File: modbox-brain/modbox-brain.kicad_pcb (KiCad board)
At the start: 2 copper layers, 100 x 40 mm, 30 parts, among them P1 MICRO-USB-B, P2 CONN_01X04, Q1 Q_PMOS_GDS, Q2 BC237, Q3 BC237, U1 MCP73831T, U2 CP2102

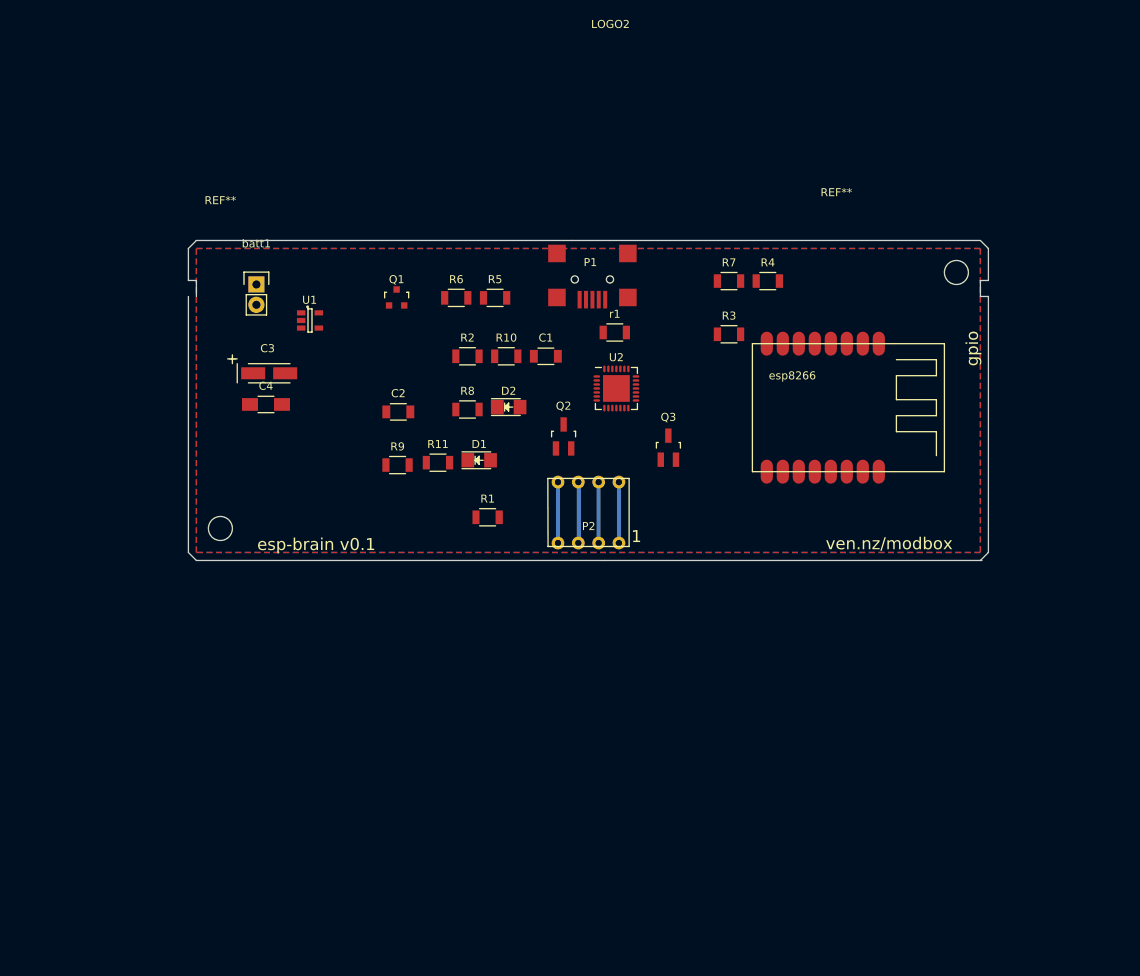
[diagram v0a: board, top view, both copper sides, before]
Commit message: buck converter instead of ldo
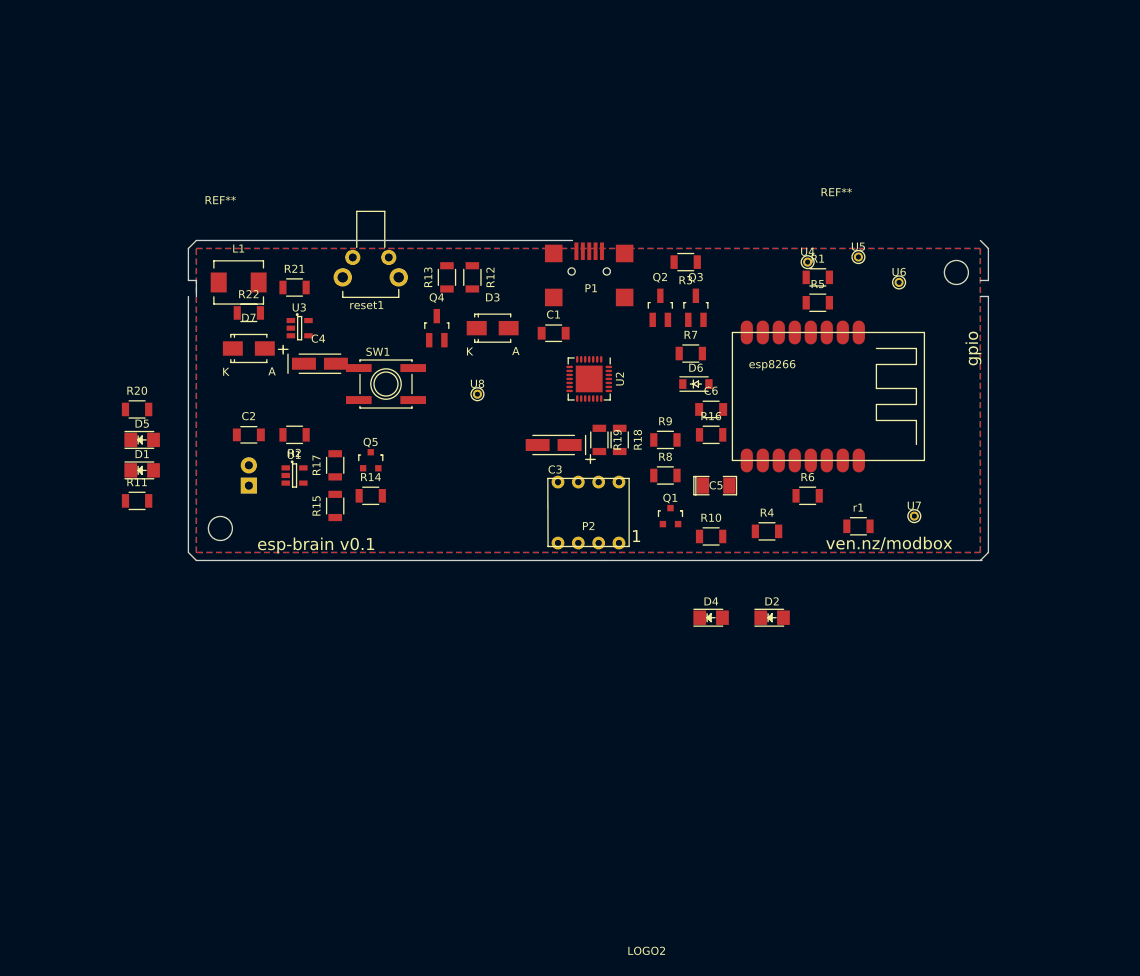
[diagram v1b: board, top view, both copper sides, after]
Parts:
- added C5: 0.1uf, SMD_Packages:SMD-1206_Pol, F.Cu at (181.0, 80.6)
- added C6: 1u, Capacitors_SMD:C_1206, F.Cu at (180.3, 71.1)
- added D3: D_Schottky, Diodes_SMD:SMA_Standard, F.Cu at (153.0, 61.0)
- added D4: low batt, LEDs:LED-1206, F.Cu at (180.3, 97.2)
- added D5: charge complete led, LEDs:LED-1206, F.Cu at (109.2, 74.9)
- added D6: D, Diodes_SMD:SOD-123, F.Cu at (178.4, 67.9)
- added D7: 1.5a, Diodes_SMD:SMA_Standard, F.Cu at (122.6, 63.5)
- added L1: 2.2u 1.8A, Inductors_NEOSID:Neosid_Inductor_SM-PIC0512H, F.Cu at (121.3, 55.2)
- added Q4: Q_PMOS_GSD, Housings_SOT-23_SOT-143_TSOT-6:SOT-23_Handsoldering, F.Cu at (146.1, 61.0)
- added Q5: Q_NMOS_GSD, TO_SOT_Packages_SMD:SOT-23, F.Cu at (137.8, 77.5)
- added R12: 30k, Resistors_SMD:R_1206, F.Cu at (150.5, 54.6)
- added R13: 60k, Resistors_SMD:R_1206, F.Cu at (147.3, 54.6)
- added R14: 10k, Resistors_SMD:R_1206, F.Cu at (137.8, 81.9)
- added R15: 4.7k, Resistors_SMD:R_1206, F.Cu at (133.3, 83.2)
- added R16: 100k, Resistors_SMD:R_1206, F.Cu at (180.3, 74.3)
- added R17: 10k, Resistors_SMD:R_1206, F.Cu at (133.3, 78.1)
- added R18: 4.7k, Resistors_SMD:R_1206, F.Cu at (168.9, 74.9)
- added R19: 4.7k, Resistors_SMD:R_1206, F.Cu at (166.4, 74.9)
- added R20: 500r, Resistors_SMD:R_1206, F.Cu at (108.6, 71.1)
- added R21: 45.3k, Resistors_SMD:R_1206, F.Cu at (128.3, 55.9)
- added R22: 100k, Resistors_SMD:R_1206, F.Cu at (122.6, 59.1)
- added SW1: SW_PUSH, Buttons_Switches_SMD:SW_SPST_EVQQ2, F.Cu at (139.7, 67.9)
- added U3: lmr1501, TO_SOT_Packages_SMD:SOT-23-5, F.Cu at (128.9, 61.0)
- added U4: testpoint, Connect:PINTST, F.Cu at (192.4, 52.7)
- added U5: testpoint, Connect:PINTST, F.Cu at (198.8, 52.1)
- added U6: testpoint, Connect:PINTST, F.Cu at (203.8, 55.2)
- added U7: testpoint, Connect:PINTST, F.Cu at (205.7, 84.5)
- added U8: testpoint, Connect:PINTST, F.Cu at (151.1, 69.2)
- added reset1: SW_PUSH, fp:ra tactile, F.Cu at (137.8, 54.6)
- C3: value 10uf -> 22uf 5v
- C4: value 0.1uf -> 22uf 10v; footprint Capacitors_SMD:C_1206_HandSoldering -> Capacitors_Tantalum_SMD:TantalC_SizeA_EIA-3216_HandSoldering
- D1: value LED -> charging led
- D2: value LED -> wifi status
- R10: value 2k -> 100k
- R9: value 2k -> 68r
- U1: value MCP73831T -> MCP73831
- batt1: moved to B.Cu
- moved LOGO2 115.9 mm to (172.2, 141.3)
- moved R1 51.0 mm to (193.7, 54.6)
- moved R6 50.4 mm to (192.4, 81.9)
- moved Q1 43.8 mm to (175.3, 84.5)
- moved D2 42.2 mm to (188.0, 97.2)
- moved D1 42.1 mm to (109.2, 78.7)
- moved R5 40.3 mm to (193.7, 57.8)
- moved r1 38.9 mm to (198.8, 85.7)
- moved R11 37.9 mm to (108.6, 82.5)
- moved C3 36.7 mm to (160.7, 75.6), turned to 180 degrees
- moved R10 34.1 mm to (180.3, 87.0)
- moved R9 33.6 mm to (174.6, 74.9)
- moved R4 31.3 mm to (187.3, 86.4)
- moved R8 26.1 mm to (174.6, 79.4)
- moved batt1 25.2 mm to (122.6, 80.6)
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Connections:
- C4 pad 1: +3V3 -> Net-(C4-Pad1)
- D1 pad 2: +5V -> Net-(D1-Pad2)
- D2 pad 2: +5V -> /gpio15
- P1 pad 1: VCC -> +5V
- R10 pad 1: adc -> +3V3
- R10 pad 2: GND -> /i2c-bus-power
- R11 pad 1: Net-(D1-Pad1) -> Net-(D1-Pad2)
- R11 pad 2: GND -> +5V
- R8 pad 2: charge -> GND
- R9 pad 1: batt -> Net-(D4-Pad2)
- R9 pad 2: adc -> +3V3
- U1 pad 1: charge -> Net-(D1-Pad1)
- U2 pad 6: (no net) -> Net-(C5-Pad2)
- U2 pad 7: VCC -> +5V
- U2 pad 8: VCC -> +5V
- esp8266 pad 13: (no net) -> /sda
- esp8266 pad 14: (no net) -> /scl
- esp8266 pad 5: (no net) -> usb-on
- esp8266 pad 7: (no net) -> power-on
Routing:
- net GND: track 7.62 -> 0.00 mm
- net /sda: track 7.62 -> 0.00 mm
- net /scl: track 7.62 -> 0.00 mm
- net Net-(P2-Pad2): track 7.58 -> 0.08 mm

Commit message: libs
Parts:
- removed LOGO2: OPEN_HARDWARE_1, Oddities:Dummy_Empty
- removed r1: 470r, Resistors_SMD:R_1206
- added C7: 0.1uf, SMD_Packages:SMD-1206_Pol, F.Cu at (184.0, 83.0)
- added D8: D, Diodes_SMD:SOD-123, F.Cu at (178.0, 69.8)
- added R23: 470r, Resistors_SMD:R_1206, F.Cu at (197.0, 83.5)
- U3: value lmr1501 -> lmr10510
- moved reset1 48.2 mm to (186.0, 55.0)
- moved C3 33.7 mm to (128.0, 84.0), turned to 0 degrees
- moved U1 32.6 mm to (153.3, 58.4)
- moved R2 32.4 mm to (153.5, 54.0)
- moved batt1 30.8 mm to (145.0, 59.5)
- moved C2 30.8 mm to (149.0, 58.5), turned to 90 degrees
- moved U7 30.7 mm to (204.2, 53.8)
- moved R9 29.9 mm to (203.2, 83.5), turned to 270 degrees
- moved D4 29.3 mm to (206.2, 83.5), turned to 90 degrees
- moved D1 27.2 mm to (123.8, 55.8), turned to 90 degrees
- moved R8 26.0 mm to (200.2, 83.5), turned to 90 degrees
- moved D2 25.7 mm to (209.8, 83.5), turned to 90 degrees
- moved R11 23.8 mm to (120.2, 61.8), turned to 270 degrees
- moved D3 23.5 mm to (129.5, 61.5)
- moved U8 22.9 mm to (174.0, 69.8)
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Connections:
- net /cp2102/D+ renamed /D+
- net /cp2102/D- renamed /D-
- net Net-(C4-Pad1) renamed /charger/dcdc-in
- net Net-(P2-Pad2) renamed /bus-power
- net Net-(R21-Pad2) renamed /charger/fb
- C6 pad 1: +5V -> /charger/enable
- D6 pad 1: +5V -> /charger/enable
- D7 pad 1: Net-(D7-Pad1) -> /charger/sw
- L1 pad 1: Net-(D7-Pad1) -> /charger/sw
- R16 pad 1: +5V -> /charger/enable
- R21 pad 1: Net-(D7-Pad1) -> +3V3
- SW1 pad 2: +5V -> /charger/enable
- U3 pad 1: Net-(D7-Pad1) -> /charger/sw
- U3 pad 4: +5V -> /charger/enable
- U7 pad 1: rx -> tx
- U8 pad 1: +5V -> /charger/enable
- esp8266 pad 15: rx -> tx
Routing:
- net +3V3: track 0.00 -> 154.3 mm, vias 0 -> 2
- net GND: track 0.00 -> 113.9 mm, vias 0 -> 4
- net +5V: track 0.00 -> 111.1 mm, vias 0 -> 3
- net rx: track 0.00 -> 76.3 mm, vias 0 -> 2
- net /charger/enable: track 0.00 -> 72.7 mm, vias 0 -> 2
- net usb-on: track 0.00 -> 67.1 mm, vias 0 -> 2
- net power-on: track 0.00 -> 66.6 mm, vias 0 -> 3
- net adc: track 0.00 -> 59.6 mm, vias 0 -> 2
- net /gpio0: track 0.00 -> 54.1 mm, vias 0 -> 1
- net /reset: track 0.00 -> 47.0 mm, vias 0 -> 2
- net batt: track 0.00 -> 44.3 mm
- net Net-(R23-Pad2): track 0.00 -> 43.0 mm, vias 0 -> 4
- net /charger/dcdc-in: track 0.00 -> 41.0 mm
- net /scl: track 0.00 -> 40.7 mm, vias 0 -> 1
- net /sda: track 0.00 -> 39.7 mm, vias 0 -> 1
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- added copper zone on F.Cu, net /charger/dcdc-in
- added copper zone on F.Cu, net /charger/sw
- added copper zone on B.Cu, net GND
- added copper zone on F.Cu, net GND
- removed copper zone on B.Cu, net Earth
- removed copper zone on F.Cu, net Earth
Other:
- net class power added: clearance 0.2, trace_width 0.5, via_dia 0.6, via_drill 0.4
- board text added: "c1"
- board text added: "stictch vias"

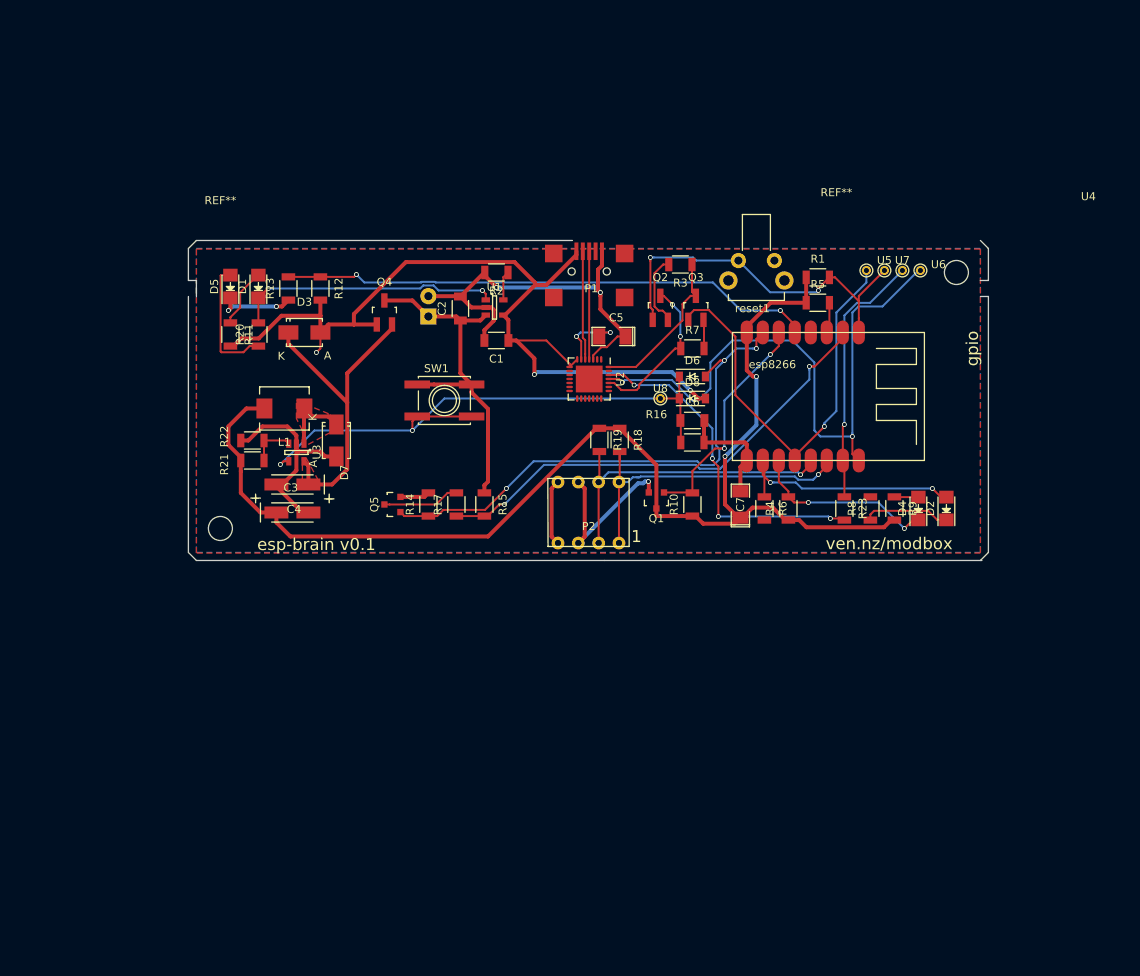
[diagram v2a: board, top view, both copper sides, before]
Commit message: fps for switcher
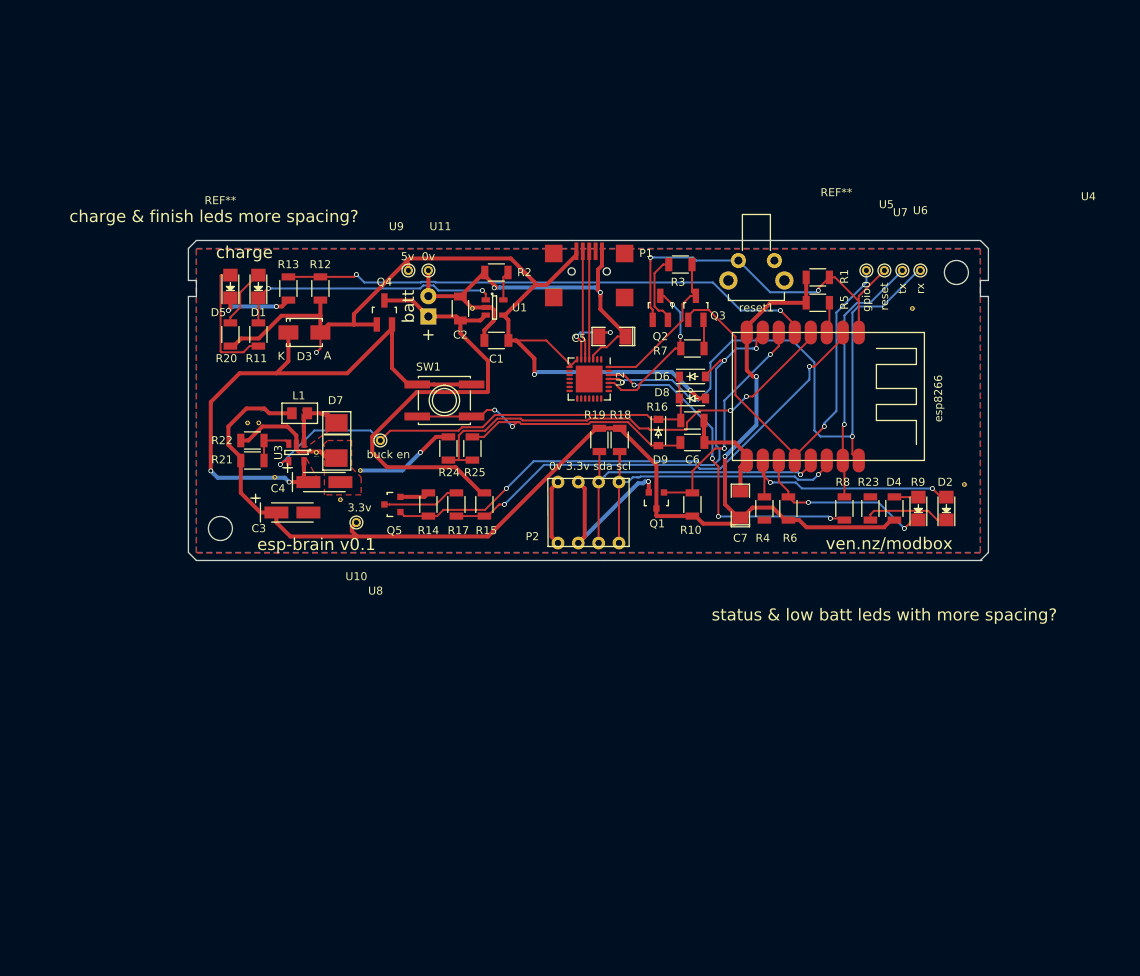
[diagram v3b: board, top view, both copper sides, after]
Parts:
- added D9: D, Diodes_SMD:SOD-123, F.Cu at (173.8, 74.0)
- added R24: 30k, Resistors_SMD:R_1206, F.Cu at (150.5, 76.0)
- added R25: 60k, Resistors_SMD:R_1206, F.Cu at (147.5, 76.0)
- added REF**1: via, fp:via, F.Cu at (136.5, 78.8)
- added REF**1: via, fp:via, F.Cu at (125.8, 79.6)
- added REF**2: via, fp:via, F.Cu at (212.0, 80.5)
- added REF**2: via, fp:via, F.Cu at (122.4, 72.8)
- added REF**3: via, fp:via, F.Cu at (205.5, 58.5)
- added REF**3: via, fp:via, F.Cu at (123.8, 72.8)
- added REF**4: via, fp:via, F.Cu at (150.5, 58.5)
- added REF**5: via, fp:via, F.Cu at (131.0, 76.5)
- added REF**5: via, fp:via, F.Cu at (134.0, 82.4)
- added U10: testpoint, Connect:PINTST, F.Cu at (136.0, 85.2)
- added U11: testpoint, Connect:PINTST, F.Cu at (145.0, 53.8)
- added U9: testpoint, Connect:PINTST, F.Cu at (142.5, 53.8)
- D7: footprint Diodes_SMD:SMA_Standard -> fp:do-214aa
- L1: footprint Inductors_NEOSID:Neosid_Inductor_SM-PIC0512H -> Microwave:CC08CC
- moved U8 35.4 mm to (139.0, 75.0)
- moved C4 4.01 mm to (132.0, 80.2), turned to 0 degrees
- moved C6 2.75 mm to (178.0, 75.2)
- moved R16 2.75 mm to (178.0, 72.5)
- moved L1 1.71 mm to (128.6, 71.6)
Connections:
- C6 pad 1: /charger/enable -> Net-(C6-Pad1)
- SW1 pad 1: batt -> /charger/dcdc-in
- SW1 pad 2: /charger/enable -> Net-(C6-Pad1)
- esp8266 pad 4: (no net) -> button
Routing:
- net button: track 0.00 -> 57.7 mm, vias 0 -> 2
- net Net-(C6-Pad1): track 0.00 -> 42.5 mm, vias 0 -> 2
- net /charger/dcdc-in: track 41.0 -> 73.1 mm, vias 0 -> 2
- net batt: track 44.3 -> 59.5 mm
- net /charger/enable: track 72.7 -> 62.3 mm, vias 2 -> 1
- net +3V3: track 154.3 -> 160.3 mm
- net GND: track 113.9 -> 118.3 mm, vias 4 -> 5
- net +5V: track 111.1 -> 112.7 mm
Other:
- net class Default: clearance 0.2 -> 0.19
- rule trace_clearance: 0.2 -> 0.19
- board text added: "+"
- board text added: "0v"
- board text added: "0v 3.3v sda scl"
- board text added: "3.3v"
- board text added: "5v"
- board text added: "batt"
- board text added: "buck en"
- board text added: "charge"
- board text added: "charge & finish leds more spacing?"
- board text added: "gpio0"
- board text added: "reset"
- board text added: "rx"
- board text added: "status & low batt leds with more spacing?"
- board text added: "tx"
- board text removed: "1"
- board text removed: "gpio"
- board text removed: "stictch vias"

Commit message: smaller diode
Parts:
- D7: footprint fp:do-214aa -> fp:sod-123w
- moved REF**1 8.08 mm to (133.8, 78.5)
- moved REF**2 7.18 mm to (124.0, 79.8)
- moved REF**5 5.27 mm to (133.9, 72.1)
- moved REF**3 4.47 mm to (128.2, 73.6)
- moved REF**1 3.64 mm to (133.9, 76.2)
- moved D7 2.20 mm to (131.8, 76.4)
- moved L1 1.41 mm to (130.0, 71.8), turned to 90 degrees
- moved C4 1.33 mm to (130.7, 80.5)
- moved REF**5 0.54 mm to (133.8, 82.9)
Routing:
- net GND: track 118.3 -> 97.9 mm
- net /charger/enable: track 62.3 -> 69.5 mm
- net /charger/sw: track 9.52 -> 5.07 mm
- net +3V3: track 160.3 -> 162.9 mm
- net batt: track 59.5 -> 60.1 mm

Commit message: component update before order
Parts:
- removed D2: wifi status, LEDs:LED-1206
- removed D4: low batt, LEDs:LED-1206
- removed R9: 68r, Resistors_SMD:R_1206
- removed the REF**1 at (133.9, 76.2)
- removed the REF**1 at (133.8, 78.5)
- removed the REF**2 at (212.0, 80.5)
- removed the REF**2 at (124.0, 79.8)
- removed the REF**3 at (205.5, 58.5)
- removed the REF**3 at (128.2, 73.6)
- removed the REF**5 at (133.9, 72.1)
- removed the REF**5 at (133.8, 82.9)
- removed SW1: SW_PUSH, Buttons_Switches_SMD:SW_SPST_EVQQ2
- added REF**1: via, fp:via, F.Cu at (134.0, 82.0)
- added REF**10: via, fp:via, F.Cu at (165.0, 67.5)
- added REF**15: via, fp:via, F.Cu at (208.0, 59.0)
- added REF**2: via, fp:via, F.Cu at (132.5, 85.0)
- added REF**20: via, fp:via, F.Cu at (206.0, 81.0)
- added REF**24: via, fp:via, F.Cu at (147.5, 68.5)
- added REF**25: via, fp:via, F.Cu at (209.5, 81.0)
- added REF**3: via, fp:via, F.Cu at (132.5, 72.5)
- added REF**5: via, fp:via, F.Cu at (149.0, 58.5)
- added REF**5: via, fp:via, F.Cu at (135.0, 52.5)
- added REF**9: via, fp:via, F.Cu at (127.5, 73.0)
- added U12: testpoint, Connect:PINTST, F.Cu at (122.0, 68.0)
- added U13: TLL-62, fp:TLL-62, F.Cu at (140.0, 70.0)
- added U14: testpoint, Connect:PINTST, F.Cu at (201.5, 84.5)
- P1: footprint fp:USB_B_MINI_SMD -> fp:usb-mini-b
- Q2, Q3: value BC237 -> BC849; footprint Housings_SOT-23_SOT-143_TSOT-6:SOT-23_Handsoldering -> SOT-23
- moved R8 58.6 mm to (145.0, 64.0), turned to 180 degrees
- moved REF**4 25.1 mm to (133.5, 77.0)
- moved C5 7.20 mm to (160.9, 60.8), turned to 0 degrees
- moved U8 1.50 mm to (139.0, 76.5)
- moved P1 0.85 mm to (165.0, 54.4), turned to 180 degrees
- moved Q3 0.57 mm to (179.0, 58.5), turned to 180 degrees
- moved Q2 0.52 mm to (174.5, 58.5)
- moved reset1 0.50 mm to (186.0, 54.5)
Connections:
- net /gpio15 renamed gpio15
- Q2 pad 1: /reset -> Net-(Q2-Pad1)
- Q2 pad 2: Net-(Q2-Pad2) -> rts
- Q2 pad 3: rts -> /reset
- Q3 pad 1: /gpio0 -> Net-(Q3-Pad1)
- Q3 pad 2: Net-(Q3-Pad2) -> dtr
- Q3 pad 3: dtr -> /gpio0
- R3 pad 2: Net-(Q2-Pad2) -> Net-(Q2-Pad1)
- R7 pad 2: Net-(Q3-Pad2) -> Net-(Q3-Pad1)
- R8 pad 1: Net-(D2-Pad1) -> GND
- R8 pad 2: GND -> Net-(R8-Pad2)
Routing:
- net gpio15: track 30.5 -> 58.3 mm
- net /charger/dcdc-in: track 73.5 -> 61.4 mm
- net +3V3: track 162.9 -> 150.9 mm
- net Net-(D2-Pad1): track 10.9 -> 0.00 mm
- net Net-(Q2-Pad2): track 9.06 -> 0.00 mm
- net Net-(Q3-Pad1): track 0.00 -> 7.55 mm
- net Net-(Q2-Pad1): track 0.00 -> 7.53 mm
- net batt: track 60.1 -> 52.7 mm
- net /gpio2: track 23.4 -> 17.6 mm, vias 2 -> 0
- net /D-: track 13.6 -> 8.26 mm
- net Net-(R8-Pad2): track 0.00 -> 5.00 mm
- net Net-(C5-Pad2): track 9.17 -> 4.70 mm, vias 2 -> 0
- net rts: track 19.6 -> 16.0 mm, vias 2 -> 0
- net Net-(Q3-Pad2): track 3.61 -> 0.00 mm
- net /reset: track 47.0 -> 43.7 mm, vias 2 -> 0
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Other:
- board text added: "15mil to board edge"
- board text added: "Matt Venn ven.nz/modbox modular controller 2016 open hardware PCBs by OSHPark.com"
- board text added: "dc/dc in"
- board text added: "en"
- board text added: "gpio2"
- board text removed: "buck en"
- board text removed: "c1"
- board text removed: "charge & finish leds more spacing?"
- board text removed: "status & low batt leds with more spacing?"

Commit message: first round of fixes post fab
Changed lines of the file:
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@@
     (tags "resistor 1206")
     (attr smd)
-    (fp_text reference R24 (at -3 -2.9 180) (layer F.SilkS)
+    (fp_text reference R24 (at -3.1 0.2 180) (layer F.SilkS)
       (effects (font (size 1 1) (thickness 0.15)))
     )
@@
     (tags "resistor 1206")
     (attr smd)
-    (fp_text reference R25 (at 3 -3.3 360) (layer F.SilkS)
+    (fp_text reference R25 (at 3.3 0.1 360) (layer F.SilkS)
       (effects (font (size 1 1) (thickness 0.15)))
     )
@@
     )
   )
-  (zone (net 27) (net_name /charger/sw) (layer B.Mask) (hatch edge 0.508)
+  (zone (net 0) (net_name "") (layer B.Mask) (hatch edge 0.508)
     (connect_pads (clearance 0.508))
     (min_thickness 0.254)
@@
     )
   )
-  (zone (net 27) (net_name /charger/sw) (layer F.Mask) (hatch edge 0.508)
+  (zone (net 0) (net_name "") (layer F.Mask) (hatch edge 0.508)
     (connect_pads (clearance 0.508))
     (min_thickness 0.254)
